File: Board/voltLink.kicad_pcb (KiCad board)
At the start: 2 copper layers, 50 x 30 mm, 43 parts, among them J1 Conn_01x06_Male, J2 Conn_01x06_Female, J3 USB_B_Micro, J4 Conn_01x08_Male, J5 Conn_01x08_Male, Q1 MBT3904DW1, U1 PUSB2X4Y, U2 CP2102N-Axx-xQFN24, U3 BU33SD5WG-TR

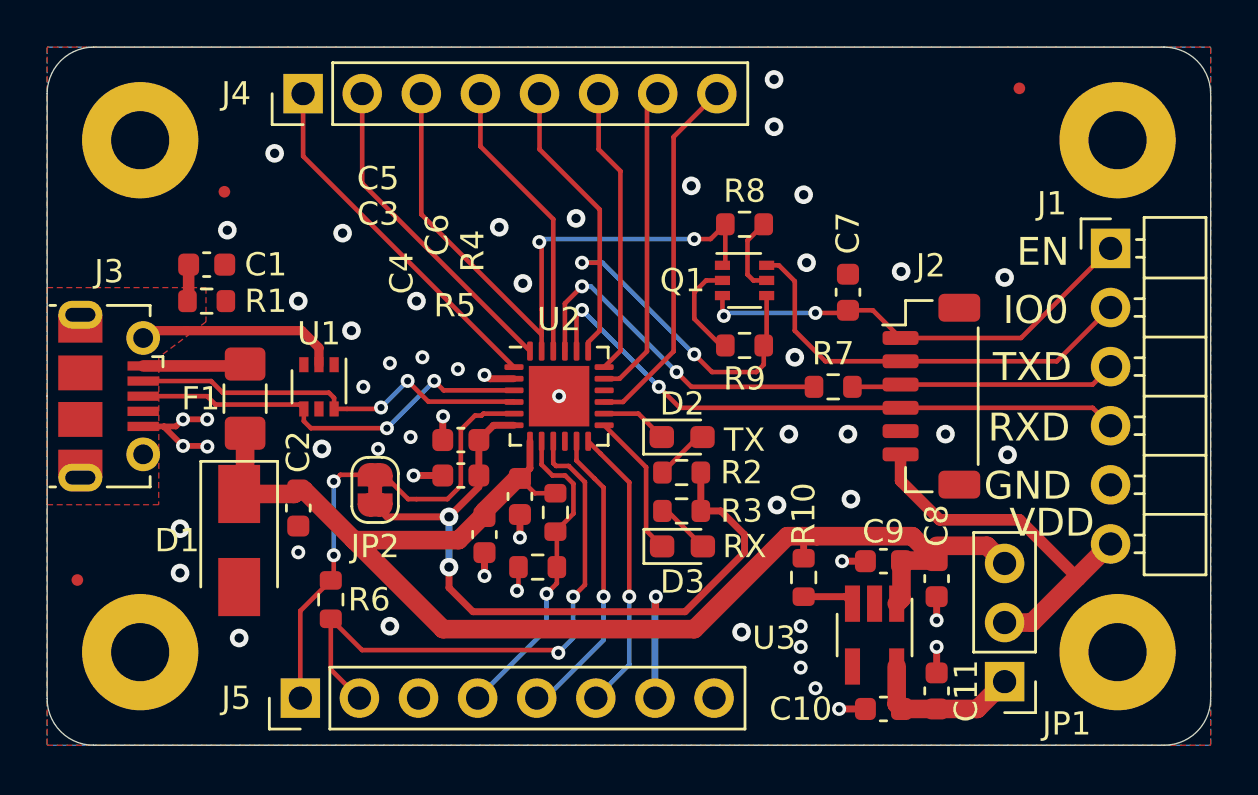
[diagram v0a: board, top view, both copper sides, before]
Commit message: Rename link to voltLink, fix KiBot export errors
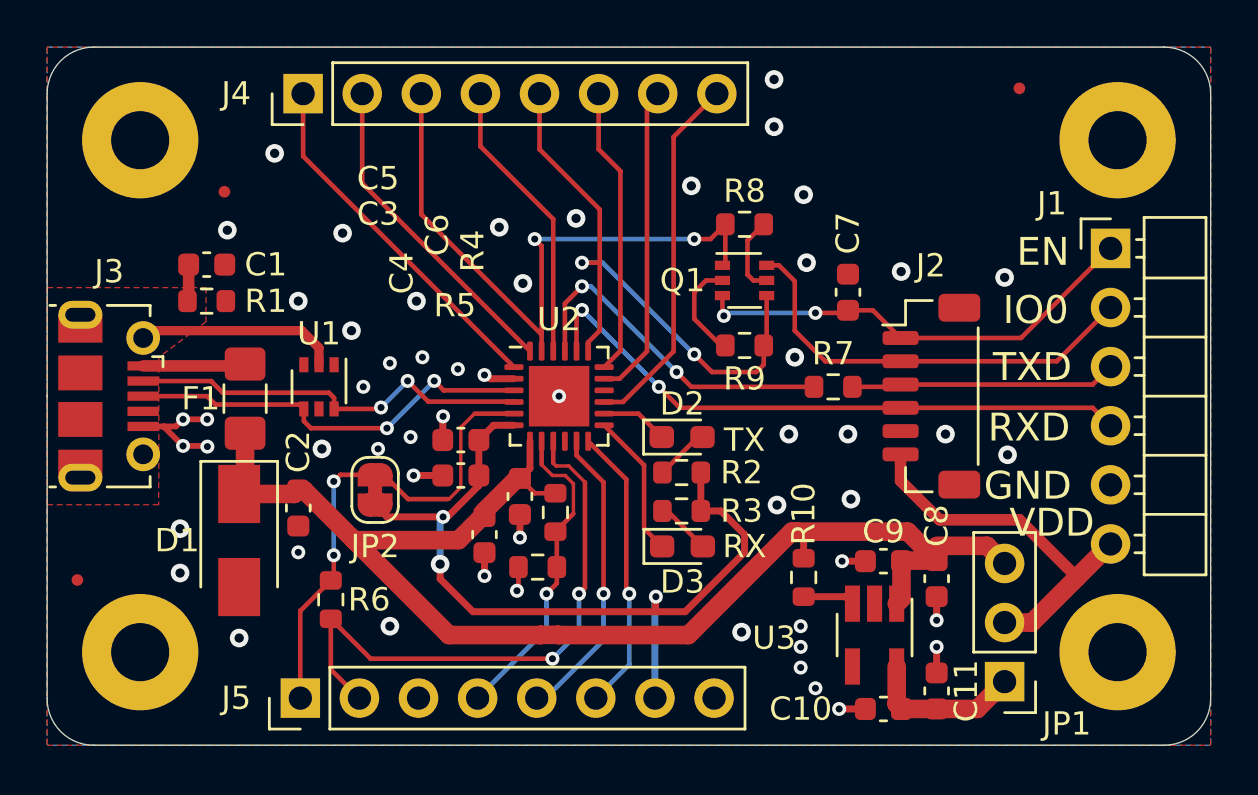
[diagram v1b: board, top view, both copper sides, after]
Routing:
- net +5V: track 56.9 -> 57.6 mm

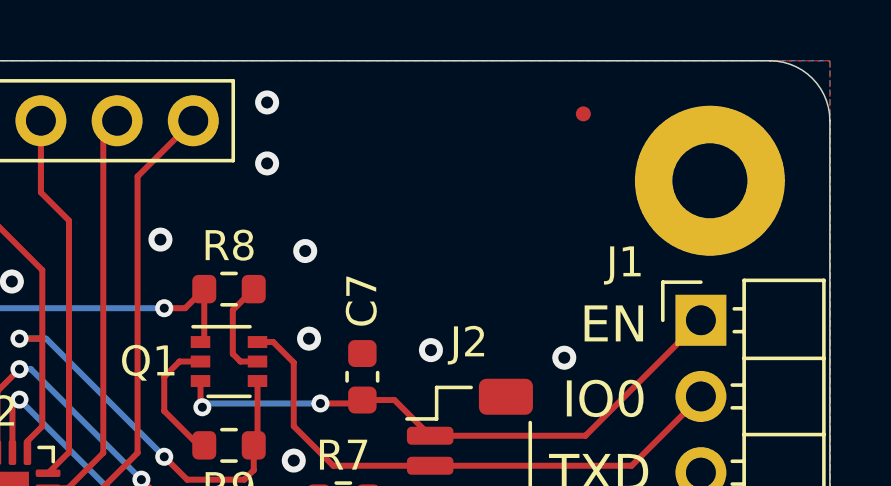
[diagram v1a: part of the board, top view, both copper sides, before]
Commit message: Add board name and version to PCB (kibuzzard)
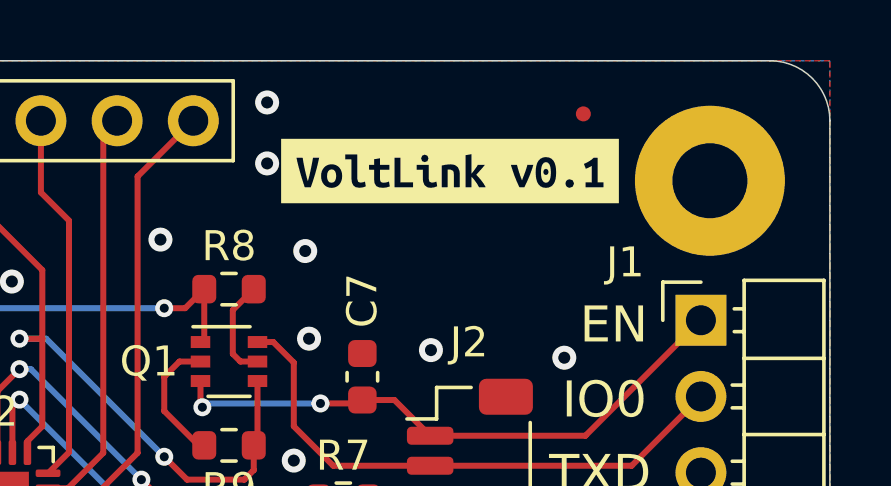
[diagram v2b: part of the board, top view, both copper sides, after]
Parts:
- added kibuzzard-61E57FAE: G***, kibuzzard-61E57FAE, F.Cu at (148.3, 74.7)

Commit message: Move some silkscreen
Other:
- board text removed: "VoltLink"
- board text removed: "revA"
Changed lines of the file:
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@@
   (gr_line (start 111 86) (end 111 99) (layer "Edge.Cuts") (width 0.05))
   (gr_line (start 159 71) (end 113 71) (layer "Edge.Cuts") (width 0.05))
-  (gr_text "VBUS" (at 121.9 94.853143 -90) (layer "B.SilkS")
+  (gr_text "VBUS" (at 121.88 94.853143 -90) (layer "B.SilkS")
     (effects (font (size 1.2 1.2) (thickness 0.25)) (justify mirror))
   )
-  (gr_text "VIO" (at 124.4 95.738857 -90) (layer "B.SilkS")
+  (gr_text "VIO" (at 124.42 95.738857 -90) (layer "B.SilkS")
     (effects (font (size 1.2 1.2) (thickness 0.25)) (justify mirror))
   )
-  (gr_text "GND" (at 126.9 95.338857 -90) (layer "B.SilkS")
+  (gr_text "GND" (at 126.96 95.338857 -90) (layer "B.SilkS")
     (effects (font (size 1.2 1.2) (thickness 0.25)) (justify mirror))
   )
@@
     (effects (font (size 1.2 1.2) (thickness 0.25)) (justify mirror))
   )
-  (gr_text "GPIO3" (at 132.1 94.481714 -90) (layer "B.SilkS")
+  (gr_text "GPIO3" (at 132.04 94.481714 -90) (layer "B.SilkS")
     (effects (font (size 1.2 1.2) (thickness 0.25)) (justify mirror))
   )
-  (gr_text "GPIO2" (at 134.6 94.481714 -90) (layer "B.SilkS")
+  (gr_text "GPIO2" (at 134.58 94.481714 -90) (layer "B.SilkS")
     (effects (font (size 1.2 1.2) (thickness 0.25)) (justify mirror))
   )
-  (gr_text "3.3V_100mA" (at 137.033 91.738857 -90) (layer "B.SilkS")
+  (gr_text "3.3V_100mA" (at 137.12 91.738857 -90) (layer "B.SilkS")
     (effects (font (size 1.2 1.2) (thickness 0.25)) (justify mirror))
   )
-  (gr_text "GND" (at 139.6 95.338857 -90) (layer "B.SilkS")
+  (gr_text "GND" (at 139.66 95.338857 -90) (layer "B.SilkS")
     (effects (font (size 1.2 1.2) (thickness 0.25)) (justify mirror))
   )
@@
     (effects (font (size 1.2 1.2) (thickness 0.25)) (justify mirror))
   )
-  (gr_text "DCD" (at 124.6 76.571429 -90) (layer "B.SilkS")
+  (gr_text "DCD" (at 124.54 76.571429 -90) (layer "B.SilkS")
     (effects (font (size 1.2 1.2) (thickness 0.25)) (justify mirror))
   )
-  (gr_text "DTR" (at 127.1 76.428572 -90) (layer "B.SilkS")
+  (gr_text "DTR" (at 127.08 76.428572 -90) (layer "B.SilkS")
     (effects (font (size 1.2 1.2) (thickness 0.25)) (justify mirror))
   )
-  (gr_text "DSR" (at 129.7 76.542857 -90) (layer "B.SilkS")
+  (gr_text "DSR" (at 129.62 76.542857 -90) (layer "B.SilkS")
     (effects (font (size 1.2 1.2) (thickness 0.25)) (justify mirror))
   )
-  (gr_text "RTS" (at 132.2 76.4 -90) (layer "B.SilkS")
+  (gr_text "RTS" (at 132.16 76.4 -90) (layer "B.SilkS")
     (effects (font (size 1.2 1.2) (thickness 0.25)) (justify mirror))
   )
-  (gr_text "CTS" (at 134.8 76.4 -90) (layer "B.SilkS")
+  (gr_text "CTS" (at 134.7 76.4 -90) (layer "B.SilkS")
     (effects (font (size 1.2 1.2) (thickness 0.25)) (justify mirror))
   )
-  (gr_text "SUS" (at 137.3 76.542857 -90) (layer "B.SilkS")
+  (gr_text "SUS" (at 137.24 76.542857 -90) (layer "B.SilkS")
     (effects (font (size 1.2 1.2) (thickness 0.25)) (justify mirror))
   )
-  (gr_text "nSUS" (at 139.8 77.085714 -90) (layer "B.SilkS")
+  (gr_text "nSUS" (at 139.78 77.085714 -90) (layer "B.SilkS")
     (effects (font (size 1.2 1.2) (thickness 0.25)) (justify mirror))
   )
-  (gr_text "5V" (at 149.86 93.218) (layer "B.SilkS")
+  (gr_text "5V" (at 149.86 93.188) (layer "B.SilkS")
     (effects (font (size 1 1) (thickness 0.15)) (justify mirror))
   )
-  (gr_text "RXD" (at 153.162 87.376) (layer "B.SilkS")
-    (effects (font (size 1.2 1.2) (thickness 0.25)) (justify mirror))
-  )
-  (gr_text "IO0" (at 153.416 82.296) (layer "B.SilkS")
-    (effects (font (size 1.2 1.2) (thickness 0.25)) (justify mirror))
-  )
-  (gr_text "EN" (at 153.797 79.756) (layer "B.SilkS")
-    (effects (font (size 1.2 1.2) (thickness 0.25)) (justify mirror))
-  )
-  (gr_text "VDD sel" (at 147.828 95.758) (layer "B.SilkS")
+  (gr_text "RXD" (at 159.258 87.27) (layer "B.SilkS")
     (effects (font (size 1 1) (thickness 0.15)) (justify mirror))
   )
-  (gr_text "3.3V" (at 149.352 98.298) (layer "B.SilkS")
+  (gr_text "IO0" (at 159.019905 82.19) (layer "B.SilkS")
     (effects (font (size 1 1) (thickness 0.15)) (justify mirror))
   )
-  (gr_text "GND" (at 153.162 89.789) (layer "B.SilkS")
-    (effects (font (size 1.2 1.2) (thickness 0.25)) (justify mirror))
+  (gr_text "EN" (at 158.758 79.65) (layer "B.SilkS")
+    (effects (font (size 1 1) (thickness 0.15)) (justify mirror))
   )
-  (gr_text "TXD" (at 153.289 84.709) (layer "B.SilkS")
-    (effects (font (size 1.2 1.2) (thickness 0.25)) (justify mirror))
+  (gr_text "VDD sel" (at 147.86 95.728) (layer "B.SilkS")
+    (effects (font (size 1 1) (thickness 0.15)) (justify mirror))
+  )
+  (gr_text "3.3V" (at 149.145714 98.268) (layer "B.SilkS")
+    (effects (font (size 1 1) (thickness 0.15)) (justify mirror))
+  )
+  (gr_text "GND" (at 159.305619 89.81) (layer "B.SilkS")
+    (effects (font (size 1 1) (thickness 0.15)) (justify mirror))
+  )
+  (gr_text "TXD" (at 159.138953 84.73) (layer "B.SilkS")
+    (effects (font (size 1 1) (thickness 0.15)) (justify mirror))
   )
   (gr_text "WWW.VOLTLOG.COM" (at 141.605 85.598 270) (layer "B.SilkS")
-    (effects (font (size 1.5 1.5) (thickness 0.3)) (justify mirror))
+    (effects (font (size 1 1) (thickness 0.15)) (justify mirror))
   )
-  (gr_text "VDD" (at 154.051 91.567) (layer "B.SilkS")
-    (effects (font (size 1.2 1.2) (thickness 0.25)) (justify mirror))
+  (gr_text "VDD" (at 159.210381 92.35) (layer "B.SilkS")
+    (effects (font (size 1 1) (thickness 0.15)) (justify mirror))
   )
   (gr_text "RXD" (at 153.197 87.35) (layer "F.SilkS")
@@
     (effects (font (size 1.2 1.2) (thickness 0.25)))
   )
-  (gr_text "VoltLink" (at 149.495 110.481 180) (layer "F.Mask")
-    (effects (font (size 1.5 1.5) (thickness 0.3) italic))
-  )
-  (gr_text "revA" (at 163.001 111.266) (layer "F.Mask")
-    (effects (font (size 1 1) (thickness 0.15)))
-  )
   (dimension (type aligned) (layer "Eco1.User")

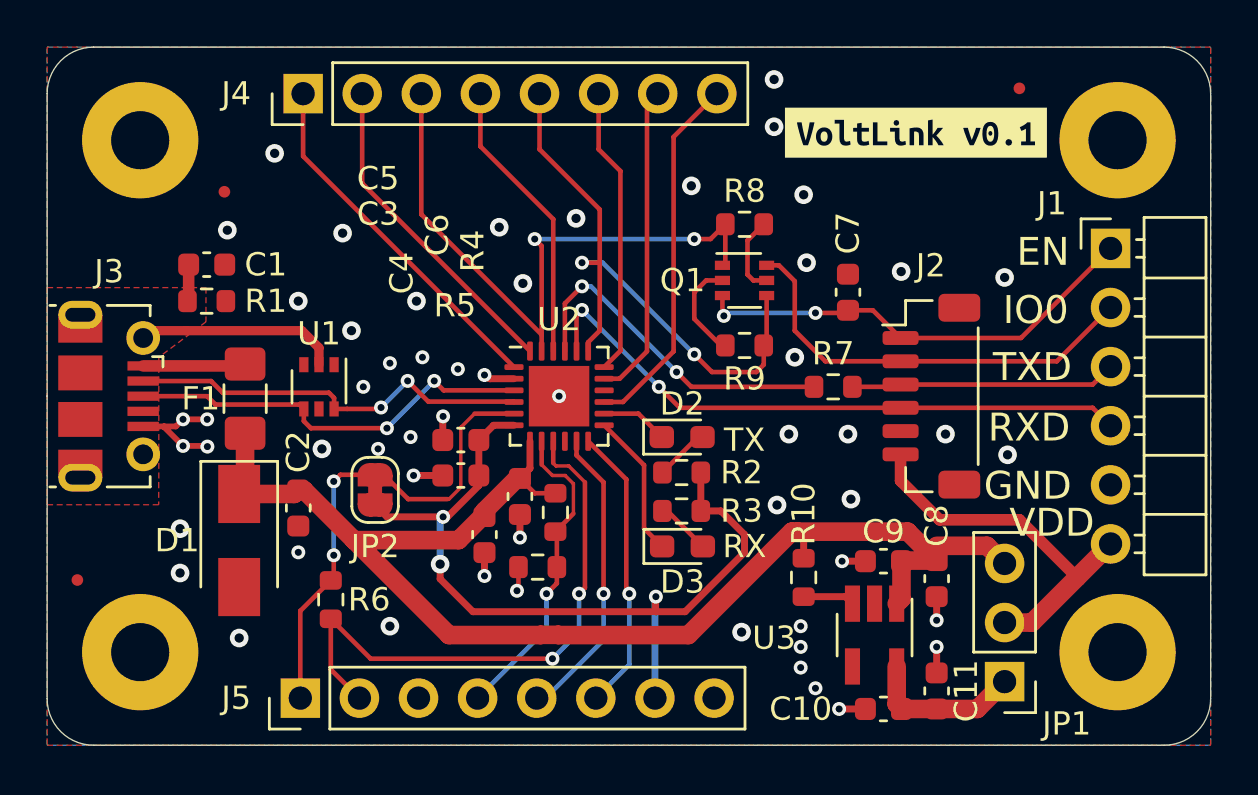
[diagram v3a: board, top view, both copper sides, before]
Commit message: Change fiducial positions
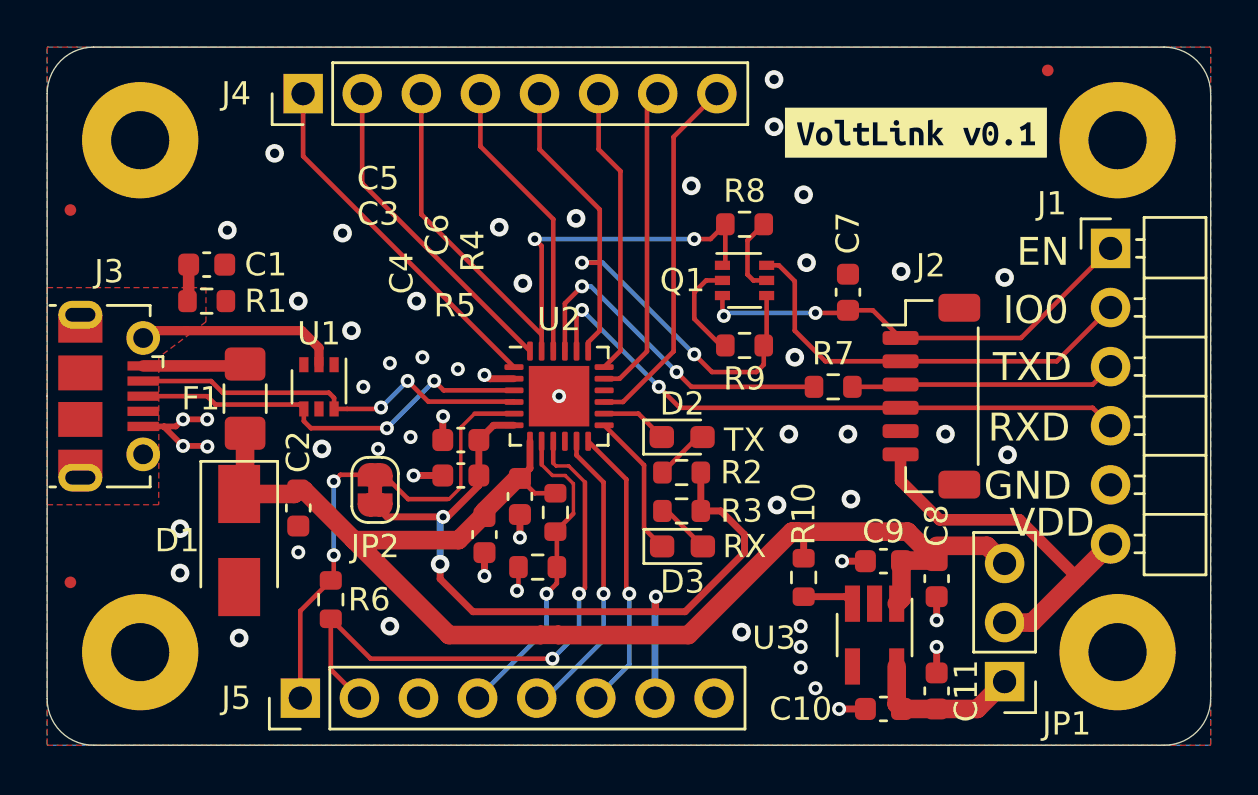
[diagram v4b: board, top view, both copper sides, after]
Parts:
- moved FID2 6.66 mm to (112.0, 78.0)
- moved FID3 1.44 mm to (154.0, 72.0)
- moved FID1 0.32 mm to (112.0, 94.0)
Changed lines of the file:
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@@
   (net 41 "unconnected-(U1-Pad3)")
   (footprint "Fiducial:Fiducial_0.5mm_Mask1mm" (layer "F.Cu")
-    (at 112.3 93.9)
+    (at 112 94)
     (descr "Circular Fiducial, 0.5mm bare copper, 1mm soldermask opening (Level C)")
     (tags "fiducial")
@@
   )
   (footprint "Fiducial:Fiducial_0.5mm_Mask1mm" (layer "F.Cu")
-    (at 118.618 77.216)
+    (at 112 78)
     (descr "Circular Fiducial, 0.5mm bare copper, 1mm soldermask opening (Level C)")
     (tags "fiducial")
@@
   )
   (footprint "Fiducial:Fiducial_0.5mm_Mask1mm" (layer "F.Cu")
-    (at 152.781 72.771)
+    (at 154 72)
     (descr "Circular Fiducial, 0.5mm bare copper, 1mm soldermask opening (Level C)")
     (tags "fiducial")
